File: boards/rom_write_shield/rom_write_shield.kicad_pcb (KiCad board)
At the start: 2 copper layers, 58.4 x 53.3 mm, 38 parts, among them J1 Conn_01x08, J2 Conn_01x06, J3 Conn_01x08, J4 Conn_01x06, J5 Conn_02x10_Top_Bottom, J6 Conn_01x02, J7 vraw_test, Q1 2SC1815, U1 LT1930, U2 LM358N

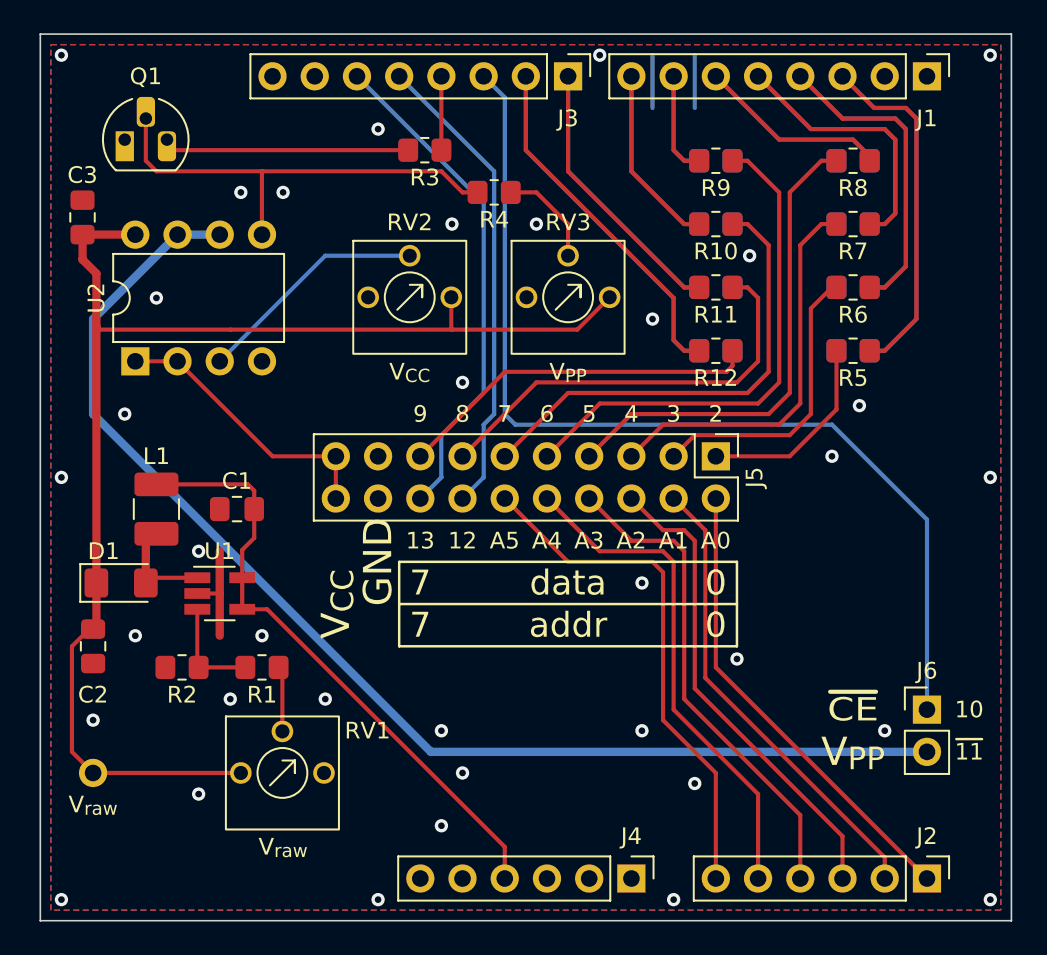
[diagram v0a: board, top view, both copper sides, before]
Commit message: adjust for creating gerver files
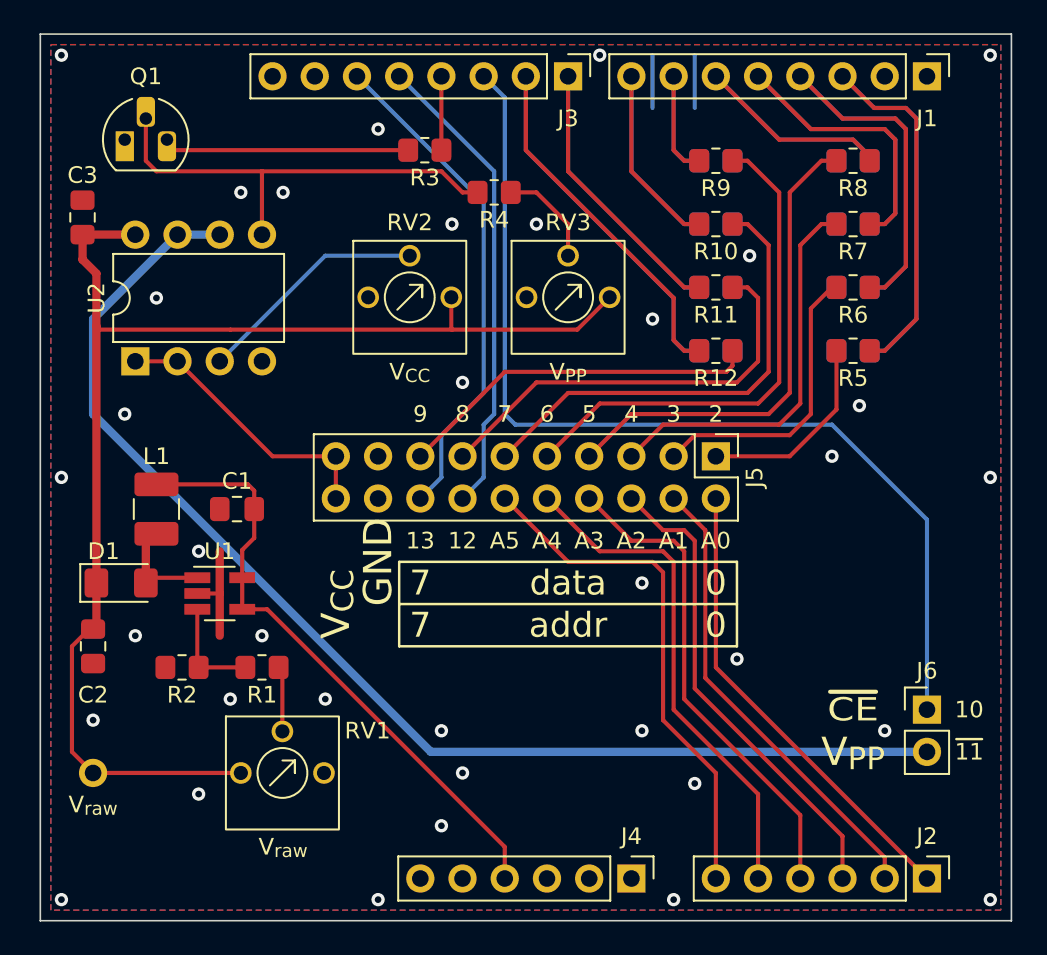
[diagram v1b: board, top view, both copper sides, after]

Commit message: unify libraries
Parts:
- J5: footprint PrjLibrary_MainBoard:PinHeader_2x10_P2.54mm_Vertical_Top_Bottom -> ModifiedKiCadLibrary:PinHeader_2x10_P2.54mm_Vertical_Top_Bottom
- RV1, RV2, RV3: footprint PrjLibrary:GF063P -> MyLibrary:GF063P
- U2: footprint PrjLibrary:DIP-8_W7.62mm_D1mm -> ModifiedKiCadLibrary:DIP-8_W7.62mm_D1mm
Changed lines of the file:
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@@
     )
   )
-  (footprint "PrjLibrary:GF063P" (layer "F.Cu")
+  (footprint "MyLibrary:GF063P" (layer "F.Cu")
     (at 136.485 102.87)
     (property "Sheetfile" "rom_write_shield.kicad_sch")
@@
       (effects (font (size 1 1) (thickness 0.15)))
     )
-    (fp_text value "100k" (at 0.04 1.27 unlocked) (layer "F.Fab")
-      (effects (font (size 1 1) (thickness 0.15)))
-    )
-    (fp_text user "${REFERENCE}" (at 0.04 2.54 unlocked) (layer "F.Fab")
-      (effects (font (size 1 1) (thickness 0.15)))
-    )
+    (fp_text value "100k" (at 0 4.5 unlocked) (layer "F.Fab")
+      (effects (font (size 1 1) (thickness 0.15)))
+    )
+    (fp_text user "${REFERENCE}" (at 0 6 unlocked) (layer "F.Fab")
+      (effects (font (size 1 1) (thickness 0.15)))
+    )
+    (fp_line (start 0.75 -0.75) (end 0 -0.75) (layer "F.SilkS") (width 0.12))
+    (fp_line (start -0.75 0.75) (end 0.75 -0.75) (layer "F.SilkS") (width 0.12))
+    (fp_line (start 0.75 0) (end 0.75 -0.75) (layer "F.SilkS") (width 0.12))
     (fp_line (start 0.75 -0.75) (end 0.75 0) (layer "F.SilkS") (width 0.12))
-    (fp_line (start 0.75 -0.75) (end 0 -0.75) (layer "F.SilkS") (width 0.12))
-    (fp_line (start 0.75 0) (end 0.75 -0.75) (layer "F.SilkS") (width 0.12))
-    (fp_line (start -0.75 0.75) (end 0.75 -0.75) (layer "F.SilkS") (width 0.12))
     (fp_rect (start -3.4 -3.4) (end 3.4 3.4) (layer "F.SilkS") (width 0.12) (fill none))
     (fp_circle (center 0 0) (end 1.5 0) (layer "F.SilkS") (width 0.12) (fill none))
@@
     )
   )
-  (footprint "PrjLibrary:GF063P" (layer "F.Cu")
+  (footprint "MyLibrary:GF063P" (layer "F.Cu")
     (at 144.145 74.255)
     (property "Sheetfile" "rom_write_shield.kicad_sch")
@@
       (effects (font (size 1 1) (thickness 0.15)))
     )
-    (fp_text value "100k" (at 0 1.31 unlocked) (layer "F.Fab")
-      (effects (font (size 1 1) (thickness 0.15)))
-    )
-    (fp_text user "${REFERENCE}" (at 0 2.81 unlocked) (layer "F.Fab")
+    (fp_text value "100k" (at 0 4.5 unlocked) (layer "F.Fab")
+      (effects (font (size 1 1) (thickness 0.15)))
+    )
+    (fp_text user "${REFERENCE}" (at 0 6 unlocked) (layer "F.Fab")
       (effects (font (size 1 1) (thickness 0.15)))
     )
     (fp_line (start 0.75 -0.75) (end 0 -0.75) (layer "F.SilkS") (width 0.12))
+    (fp_line (start 0.75 -0.75) (end 0.75 0) (layer "F.SilkS") (width 0.12))
     (fp_line (start 0.75 0) (end 0.75 -0.75) (layer "F.SilkS") (width 0.12))
     (fp_line (start -0.75 0.75) (end 0.75 -0.75) (layer "F.SilkS") (width 0.12))
-    (fp_line (start 0.75 -0.75) (end 0.75 0) (layer "F.SilkS") (width 0.12))
     (fp_rect (start -3.4 -3.4) (end 3.4 3.4) (layer "F.SilkS") (width 0.12) (fill none))
     (fp_circle (center 0 0) (end 1.5 0) (layer "F.SilkS") (width 0.12) (fill none))
@@
     )
   )
-  (footprint "PrjLibrary_MainBoard:PinHeader_2x10_P2.54mm_Vertical_Top_Bottom" (layer "F.Cu")
+  (footprint "ModifiedKiCadLibrary:PinHeader_2x10_P2.54mm_Vertical_Top_Bottom" (layer "F.Cu")
     (at 162.56 83.82 -90)
     (descr "Through hole straight pin header, 2x10, 2.54mm pitch, double rows (modified from KiCad 6 library)")
@@
     (property "Sheetname" "")
     (attr through_hole)
-    (fp_text reference "J5" (at 1.27 -2.33 90) (layer "F.SilkS")
-      (effects (font (size 1 1) (thickness 0.15)))
-    )
-    (fp_text value "Conn_02x10_Top_Bottom" (at 1.27 25.19 90) (layer "F.Fab")
+    (fp_text reference "J5" (at 1.27 -2.33 -90) (layer "F.SilkS")
+      (effects (font (size 1 1) (thickness 0.15)))
+    )
+    (fp_text value "Conn_02x10_Top_Bottom" (at 1.27 25.19 -90) (layer "F.Fab")
       (effects (font (size 1 1) (thickness 0.15)))
     )
@@
     )
     (fp_line (start -1.33 1.27) (end 1.27 1.27) (layer "F.SilkS") (width 0.12))
+    (fp_line (start 1.27 -1.33) (end 3.87 -1.33) (layer "F.SilkS") (width 0.12))
+    (fp_line (start -1.33 -1.33) (end 0 -1.33) (layer "F.SilkS") (width 0.12))
     (fp_line (start -1.33 1.27) (end -1.33 24.19) (layer "F.SilkS") (width 0.12))
-    (fp_line (start 1.27 -1.33) (end 3.87 -1.33) (layer "F.SilkS") (width 0.12))
-    (fp_line (start 1.27 1.27) (end 1.27 -1.33) (layer "F.SilkS") (width 0.12))
-    (fp_line (start -1.33 0) (end -1.33 -1.33) (layer "F.SilkS") (width 0.12))
     (fp_line (start 3.87 -1.33) (end 3.87 24.19) (layer "F.SilkS") (width 0.12))
     (fp_line (start -1.33 24.19) (end 3.87 24.19) (layer "F.SilkS") (width 0.12))
-    (fp_line (start -1.33 -1.33) (end 0 -1.33) (layer "F.SilkS") (width 0.12))
+    (fp_line (start -1.33 0) (end -1.33 -1.33) (layer "F.SilkS") (width 0.12))
+    (fp_line (start 1.27 1.27) (end 1.27 -1.33) (layer "F.SilkS") (width 0.12))
     (fp_line (start -1.8 24.65) (end 4.35 24.65) (layer "F.CrtYd") (width 0.05))
+    (fp_line (start 4.35 -1.8) (end -1.8 -1.8) (layer "F.CrtYd") (width 0.05))
+    (fp_line (start -1.8 -1.8) (end -1.8 24.65) (layer "F.CrtYd") (width 0.05))
     (fp_line (start 4.35 24.65) (end 4.35 -1.8) (layer "F.CrtYd") (width 0.05))
-    (fp_line (start -1.8 -1.8) (end -1.8 24.65) (layer "F.CrtYd") (width 0.05))
-    (fp_line (start 4.35 -1.8) (end -1.8 -1.8) (layer "F.CrtYd") (width 0.05))
     (fp_line (start 3.81 24.13) (end -1.27 24.13) (layer "F.Fab") (width 0.1))
     (fp_line (start 3.81 -1.27) (end 3.81 24.13) (layer "F.Fab") (width 0.1))
     (fp_line (start -1.27 24.13) (end -1.27 0) (layer "F.Fab") (width 0.1))
+    (fp_line (start -1.27 0) (end 0 -1.27) (layer "F.Fab") (width 0.1))
     (fp_line (start 0 -1.27) (end 3.81 -1.27) (layer "F.Fab") (width 0.1))
-    (fp_line (start -1.27 0) (end 0 -1.27) (layer "F.Fab") (width 0.1))
     (pad "1" thru_hole rect (at 0 0 270) (size 1.7 1.7) (drill 1) (layers *.Cu *.Mask)
       (net 29 "/data0") (pinfunction "Pin_1") (pintype "passive"))
@@
     )
   )
-  (footprint "PrjLibrary:GF063P" (layer "F.Cu")
+  (footprint "MyLibrary:GF063P" (layer "F.Cu")
     (at 153.67 74.255)
     (property "Sheetfile" "rom_write_shield.kicad_sch")
@@
       (effects (font (size 1 1) (thickness 0.15)))
     )
-    (fp_text value "100k" (at 0 1.31 unlocked) (layer "F.Fab")
-      (effects (font (size 1 1) (thickness 0.15)))
-    )
-    (fp_text user "${REFERENCE}" (at 0 2.81 unlocked) (layer "F.Fab")
+    (fp_text value "100k" (at 0 4.5 unlocked) (layer "F.Fab")
+      (effects (font (size 1 1) (thickness 0.15)))
+    )
+    (fp_text user "${REFERENCE}" (at 0 6 unlocked) (layer "F.Fab")
       (effects (font (size 1 1) (thickness 0.15)))
     )
     (fp_line (start 0.75 -0.75) (end 0.75 0) (layer "F.SilkS") (width 0.12))
+    (fp_line (start -0.75 0.75) (end 0.75 -0.75) (layer "F.SilkS") (width 0.12))
     (fp_line (start 0.75 -0.75) (end 0 -0.75) (layer "F.SilkS") (width 0.12))
-    (fp_line (start -0.75 0.75) (end 0.75 -0.75) (layer "F.SilkS") (width 0.12))
     (fp_line (start 0.75 0) (end 0.75 -0.75) (layer "F.SilkS") (width 0.12))
     (fp_rect (start -3.4 -3.4) (end 3.4 3.4) (layer "F.SilkS") (width 0.12) (fill none))
@@
     )
   )
-  (footprint "PrjLibrary:DIP-8_W7.62mm_D1mm" (layer "F.Cu")
+  (footprint "ModifiedKiCadLibrary:DIP-8_W7.62mm_D1mm" (layer "F.Cu")
     (at 127.635 78.105 90)
     (descr "8-lead though-hole mounted DIP package, row spacing 7.62 mm (300 mils) (modified from KiCad 6 library)")
@@
       (effects (font (size 1 1) (thickness 0.15)))
     )
-    (fp_line (start 6.46 -1.33) (end 4.81 -1.33) (layer "F.SilkS") (width 0.12))
+    (fp_line (start 2.81 -1.33) (end 1.16 -1.33) (layer "F.SilkS") (width 0.12))
     (fp_line (start 6.46 8.95) (end 6.46 -1.33) (layer "F.SilkS") (width 0.12))
     (fp_line (start 1.16 8.95) (end 6.46 8.95) (layer "F.SilkS") (width 0.12))
+    (fp_line (start 6.46 -1.33) (end 4.81 -1.33) (layer "F.SilkS") (width 0.12))
     (fp_line (start 1.16 -1.33) (end 1.16 8.95) (layer "F.SilkS") (width 0.12))
-    (fp_line (start 2.81 -1.33) (end 1.16 -1.33) (layer "F.SilkS") (width 0.12))
     (fp_arc (start 4.81 -1.33) (mid 3.81 -0.33) (end 2.81 -1.33) (layer "F.SilkS") (width 0.12))
+    (fp_line (start -1.1 9.15) (end 8.7 9.15) (layer "F.CrtYd") (width 0.05))
     (fp_line (start -1.1 -1.55) (end -1.1 9.15) (layer "F.CrtYd") (width 0.05))
-    (fp_line (start -1.1 9.15) (end 8.7 9.15) (layer "F.CrtYd") (width 0.05))
+    (fp_line (start 8.7 -1.55) (end -1.1 -1.55) (layer "F.CrtYd") (width 0.05))
     (fp_line (start 8.7 9.15) (end 8.7 -1.55) (layer "F.CrtYd") (width 0.05))
-    (fp_line (start 8.7 -1.55) (end -1.1 -1.55) (layer "F.CrtYd") (width 0.05))
+    (fp_line (start 6.985 -1.27) (end 6.985 8.89) (layer "F.Fab") (width 0.1))
+    (fp_line (start 0.635 -0.27) (end 1.635 -1.27) (layer "F.Fab") (width 0.1))
+    (fp_line (start 6.985 8.89) (end 0.635 8.89) (layer "F.Fab") (width 0.1))
     (fp_line (start 1.635 -1.27) (end 6.985 -1.27) (layer "F.Fab") (width 0.1))
     (fp_line (start 0.635 8.89) (end 0.635 -0.27) (layer "F.Fab") (width 0.1))
-    (fp_line (start 6.985 8.89) (end 0.635 8.89) (layer "F.Fab") (width 0.1))
-    (fp_line (start 0.635 -0.27) (end 1.635 -1.27) (layer "F.Fab") (width 0.1))
-    (fp_line (start 6.985 -1.27) (end 6.985 8.89) (layer "F.Fab") (width 0.1))
     (pad "1" thru_hole rect (at 0 0 90) (size 1.7 1.7) (drill 1) (layers *.Cu *.Mask)
       (net 37 "/vccout") (pintype "output"))
